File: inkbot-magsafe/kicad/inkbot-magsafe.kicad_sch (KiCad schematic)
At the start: 79 parts, among them J1 GDEY0397T81P panel FPC, J2 Protected battery + NTC, J3 WR222230 coil + bonded NTC, Q1 Si1308EDL-T1-GE3, Q2 2N7002BK,215, U1 MDBT50Q-1MV2, U2 BQ51013C, U3 BQ25186DLHR, U4 TPS7A2030PDBVR, U5 TPS7A0230PDBVR, Y1 FC-135 32.768kHz 12.5pF

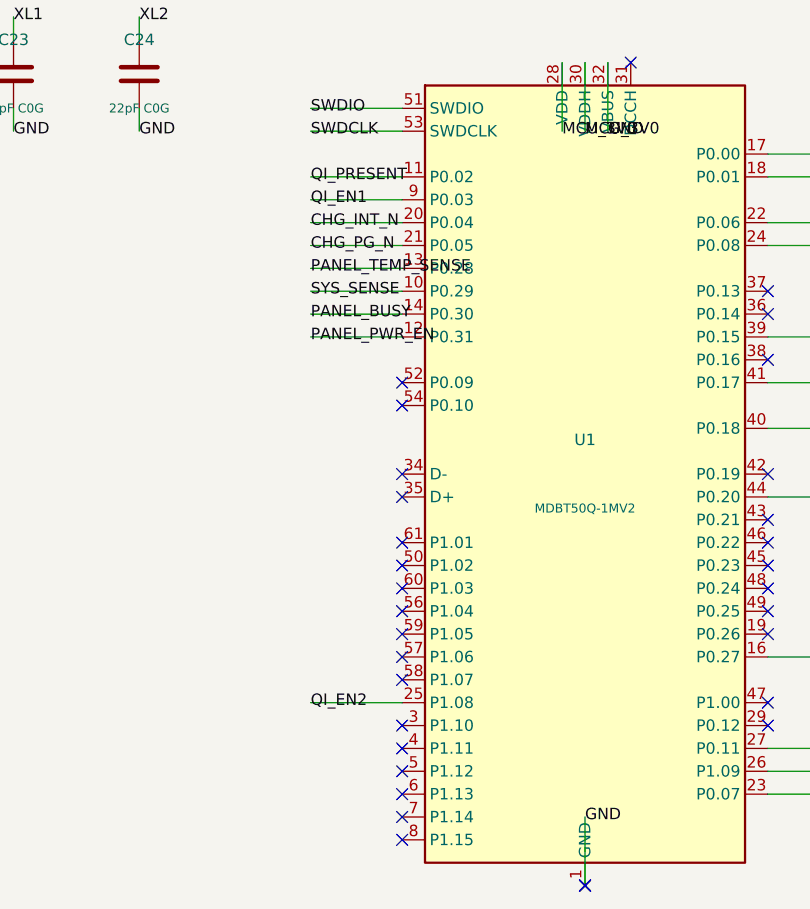
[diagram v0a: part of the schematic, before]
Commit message: inkbot-magsafe: swap status and temperature pins
Co-authored-by: Jason Hall <imjasonh@users.noreply.github.com>
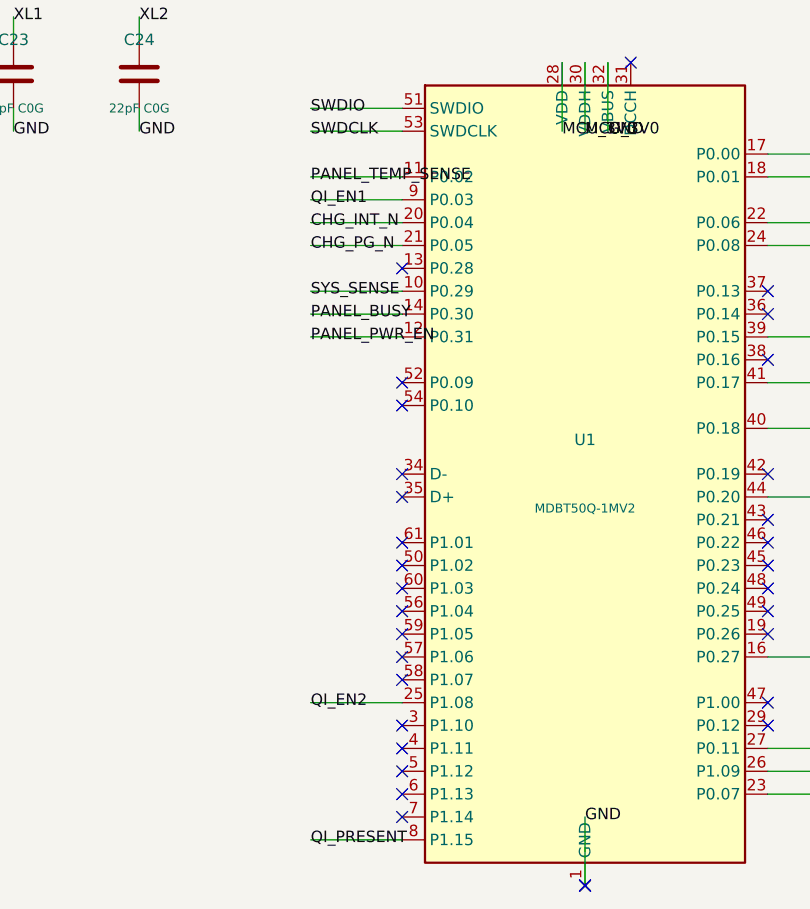
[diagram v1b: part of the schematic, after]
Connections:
- net PANEL_TEMP_SENSE: now also U1.11 (P0.02); no longer U1.13 (P0.28)
- net QI_PRESENT: now also U1.8 (P1.15); no longer U1.11 (P0.02)
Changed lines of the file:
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@@
+    (stroke (width 0) (type default))
+  )
+  (wire (pts (xy 134.62 275.59) (xy 124.46 275.59))
     (stroke (width 0) (type default))
   )
@@
     (stroke (width 0) (type default))
   )
-  (wire (pts (xy 134.62 212.09) (xy 124.46 212.09))
-    (stroke (width 0) (type default))
-  )
   (wire (pts (xy 134.62 217.17) (xy 124.46 217.17))
     (stroke (width 0) (type default))
@@
     (effects (font (size 1.27 1.27)) (justify left))
   )
+  (label "QI_PRESENT" (at 124.46 275.59 0)
+    (effects (font (size 1.27 1.27)) (justify left))
+  )
   (label "QI_EN1" (at 124.46 204.47 0)
     (effects (font (size 1.27 1.27)) (justify left))
@@
     (effects (font (size 1.27 1.27)) (justify left))
   )
-  (label "QI_PRESENT" (at 124.46 201.93 0)
+  (label "PANEL_TEMP_SENSE" (at 124.46 201.93 0)
     (effects (font (size 1.27 1.27)) (justify left))
   )
@@
     (effects (font (size 1.27 1.27)) (justify left))
   )
-  (label "PANEL_TEMP_SENSE" (at 124.46 212.09 0)
-    (effects (font (size 1.27 1.27)) (justify left))
-  )
   (label "PANEL_BUSY" (at 124.46 217.17 0)
     (effects (font (size 1.27 1.27)) (justify left))
@@
   (no_connect (at 104.14 67.31)
   )
+  (no_connect (at 134.62 212.09)
+  )
   (no_connect (at 154.94 280.67)
   )
@@
   (no_connect (at 134.62 273.05)
   )
-  (no_connect (at 134.62 275.59)
-  )
   (no_connect (at 74.93 149.86)

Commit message: inkbot-magsafe: commit clean routed board
Co-authored-by: Jason Hall <imjasonh@users.noreply.github.com>
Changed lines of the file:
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@@
-    )
-  )
-  (symbol (lib_id "power:GND") (at 204.47 119.38 0)
-    (property "Reference" "#PWR001" (at 204.47 121.92 0)
-      (effects (font (size 1.27 1.27)) hide))
-    (property "Value" "GND" (at 204.47 123.19 0)
-      (effects (font (size 0.8 0.8))))
-    (property "Footprint" "" (at 204.47 119.38 0)
-      (effects (font (size 1.27 1.27)) hide))
-    (instances
-      (project "inkbot-magsafe"
-        (path "/876e0bc8-f839-529d-8fb7-fca7b9334b7c" (reference "#PWR001") (unit 1))
-      )
     )
   )

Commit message: inkbot-magsafe: drive generated ground net
Co-authored-by: Jason Hall <imjasonh@users.noreply.github.com>
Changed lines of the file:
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@@
     )
   )
+  (symbol (lib_id "power:PWR_FLAG") (at 204.47 119.38 0)
+    (property "Reference" "#FLG001" (at 204.47 121.92 0)
+      (effects (font (size 1.27 1.27)) hide))
+    (property "Value" "PWR_FLAG" (at 204.47 123.19 0)
+      (effects (font (size 0.8 0.8))))
+    (property "Footprint" "" (at 204.47 119.38 0)
+      (effects (font (size 1.27 1.27)) hide))
+    (instances
+      (project "inkbot-magsafe"
+        (path "/876e0bc8-f839-529d-8fb7-fca7b9334b7c" (reference "#FLG001") (unit 1))
+      )
+    )
+  )
   (wire (pts (xy 91.44 92.71) (xy 91.44 85.09))
     (stroke (width 0) (type default))
@@
     (effects (font (size 1.27 1.27)) (justify left))
   )
+  (label "GND" (at 204.47 119.38 0)
+    (effects (font (size 1.27 1.27)) (justify left))
+  )

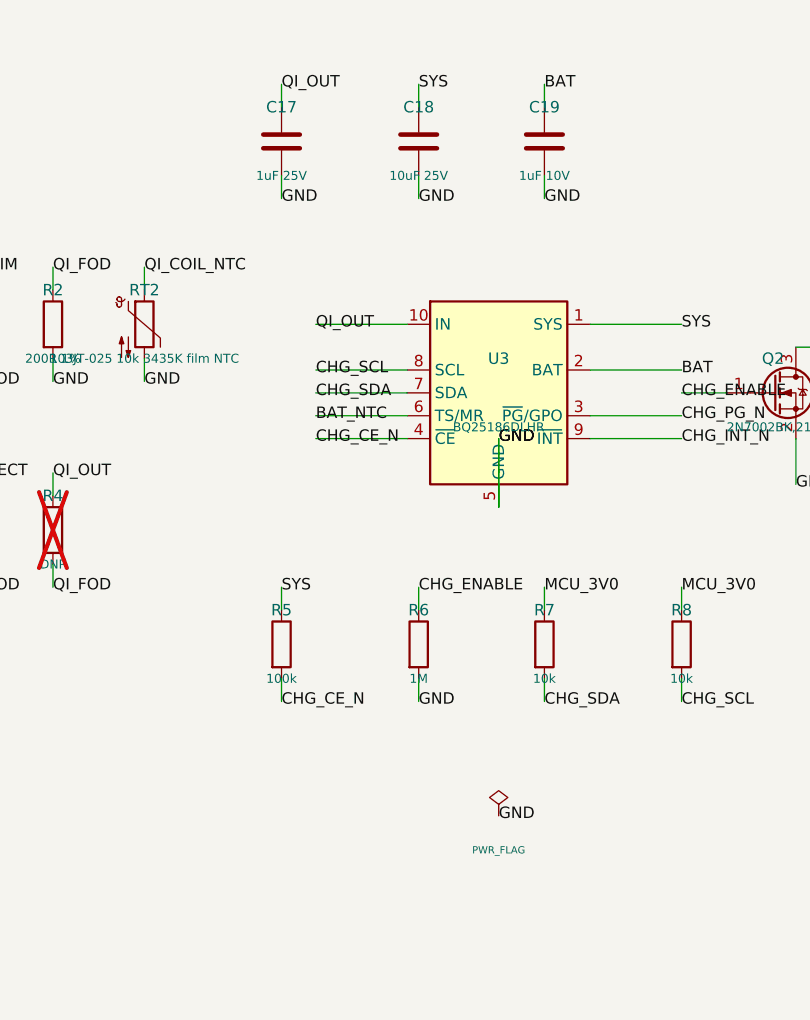
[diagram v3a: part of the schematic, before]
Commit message: inkbot-magsafe: connect the ground ERC anchor
Co-authored-by: Jason Hall <imjasonh@users.noreply.github.com>
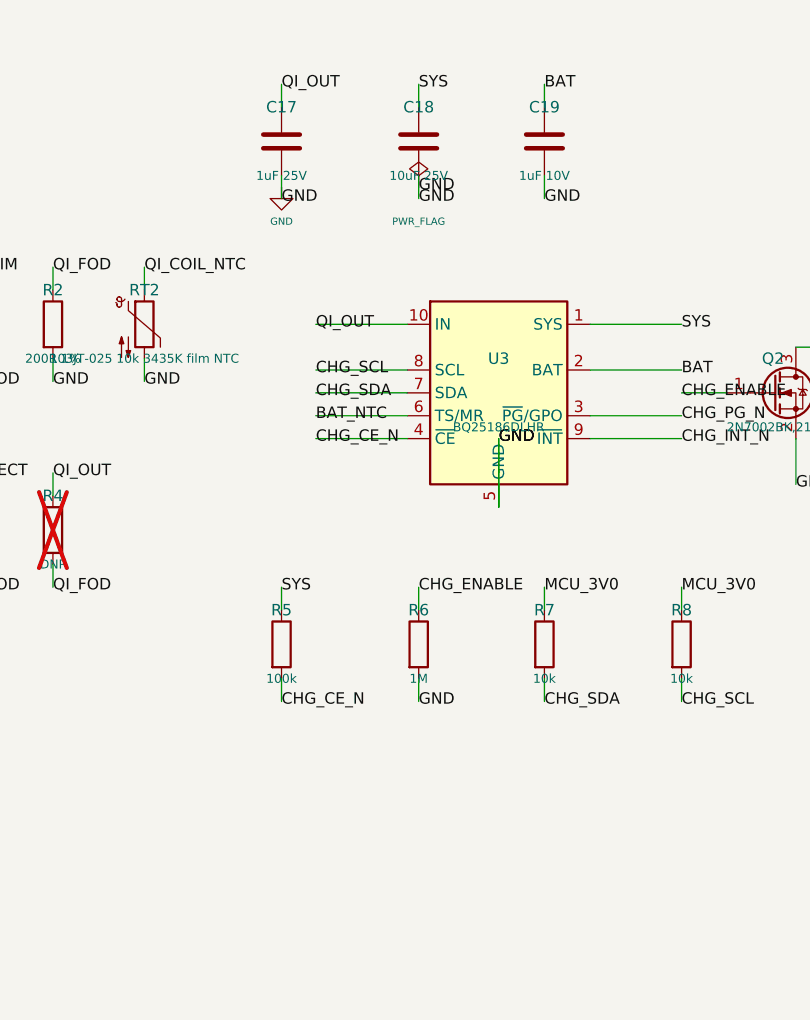
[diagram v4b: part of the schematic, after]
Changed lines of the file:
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@@
     )
   )
-  (symbol (lib_id "power:PWR_FLAG") (at 204.47 119.38 0)
-    (property "Reference" "#FLG001" (at 204.47 121.92 0)
+  (symbol (lib_id "power:GND") (at 180.34 49.53 0)
+    (property "Reference" "#PWR001" (at 180.34 52.07 0)
       (effects (font (size 1.27 1.27)) hide))
-    (property "Value" "PWR_FLAG" (at 204.47 123.19 0)
+    (property "Value" "GND" (at 180.34 53.34 0)
       (effects (font (size 0.8 0.8))))
-    (property "Footprint" "" (at 204.47 119.38 0)
+    (property "Footprint" "" (at 180.34 49.53 0)
+      (effects (font (size 1.27 1.27)) hide))
+    (instances
+      (project "inkbot-magsafe"
+        (path "/876e0bc8-f839-529d-8fb7-fca7b9334b7c" (reference "#PWR001") (unit 1))
+      )
+    )
+  )
+  (symbol (lib_id "power:PWR_FLAG") (at 195.58 49.53 0)
+    (property "Reference" "#FLG001" (at 195.58 52.07 0)
+      (effects (font (size 1.27 1.27)) hide))
+    (property "Value" "PWR_FLAG" (at 195.58 53.34 0)
+      (effects (font (size 0.8 0.8))))
+    (property "Footprint" "" (at 195.58 49.53 0)
       (effects (font (size 1.27 1.27)) hide))
     (instances
@@
     (effects (font (size 1.27 1.27)) (justify left))
   )
-  (label "GND" (at 204.47 119.38 0)
-    (effects (font (size 1.27 1.27)) (justify left))
-  )
+  (label "GND" (at 195.58 49.53 0)
+    (effects (font (size 1.27 1.27)) (justify left))
+  )

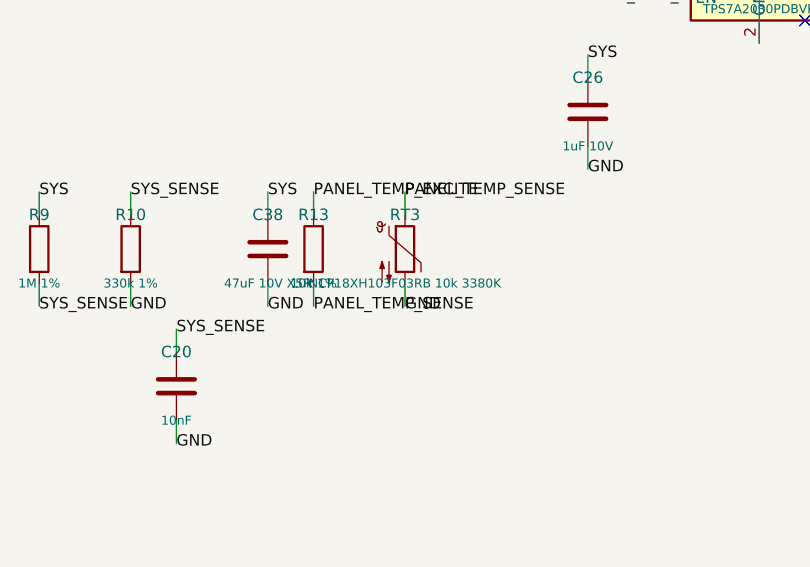
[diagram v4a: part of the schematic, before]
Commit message: inkbot-magsafe: replace NRND panel thermistor
Co-authored-by: Jason Hall <imjasonh@users.noreply.github.com>
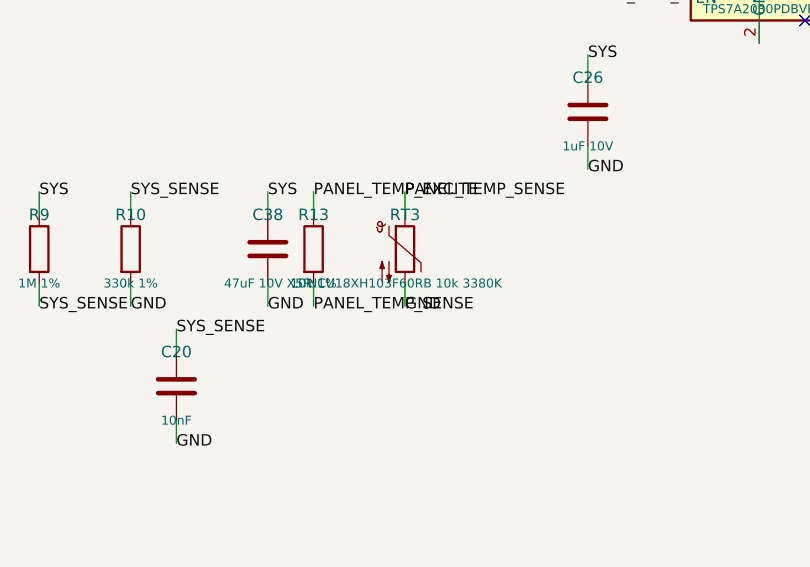
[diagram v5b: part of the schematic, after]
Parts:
- RT3: value NCP18XH103F03RB 10k 3380K -> NCU18XH103F60RB 10k 3380K
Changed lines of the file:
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@@
     (property "Reference" "RT3" (at 245.11 171.45 0)
       (effects (font (size 1.27 1.27))))
-    (property "Value" "NCP18XH103F03RB 10k 3380K" (at 245.11 179.07 0)
+    (property "Value" "NCU18XH103F60RB 10k 3380K" (at 245.11 179.07 0)
       (effects (font (size 1.0 1.0))))
     (property "Footprint" "Capacitor_SMD:C_0603_1608Metric" (at 245.11 180.34 0)
